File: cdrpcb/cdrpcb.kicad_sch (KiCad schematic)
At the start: 42 parts, among them J1 Conn_02x04_Odd_Even, J2 Conn_01x03, J3 Conn_01x03, J4 Conn_01x03, J5 Conn_01x03, J6 Conn_01x03, J7 Conn_01x06, J8 Conn_01x05, J9 Conn_01x03, SW1 SW_Push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

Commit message: update cdrpcb
bno055 footprints
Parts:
- removed SW1, SW2, SW3, SW4, SW5: SW_Push, Button_Switch_THT:SW_PUSH_6mm, symbol Switch:SW_Push
- added SW1, SW3: SW_Push, Connector_PinHeader_2.54mm:PinHeader_1x01_P2.54mm_Vertical, symbol Connector:Conn_01x01_Pin
- added SW2, SW4, SW5: SW_Push, Connector_PinHeader_2.54mm:PinHeader_1x02_P2.54mm_Vertical, symbol Connector:Conn_01x01_Pin
- added TP1: ~, TP4056:TP4056-18650, symbol TP4056:TP4056
- C1: footprint Capacitor_THT:CP_Radial_D4.0mm_P1.50mm -> Connector_PinHeader_2.54mm:PinHeader_1x02_P2.54mm_Horizontal
- U1: footprint Package_LGA:LGA-28_5.2x3.8mm_P0.5mm -> Library:BNO055_Breakout
- U2: footprint SC0918:MODULE_SC0918 -> RP2040_SC0918:MODULE_SC0918
- U3: footprint PDIP8_300MC_MCH -> 25LC1024:PDIP8_300MC_MCH
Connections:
- net RST: now also SW1.1 (Pin_1)
- net SW0: now also SW2.1 (Pin_1)
- net SW1: now also SW3.1 (Pin_1)
- net SW2: now also SW4.1 (Pin_1), SW5.1 (Pin_1)

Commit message: cdrpcb3
Started routing
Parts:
- removed C6, C7: 100nF, Capacitor_THT:CP_Radial_D4.0mm_P1.50mm, symbol Device:C
- removed J6: Conn_01x03, Connector_PinHeader_2.54mm:PinHeader_1x03_P2.54mm_Vertical, symbol Connector_Generic:Conn_01x03
- removed J8: Conn_01x05, Connector_PinHeader_2.54mm:PinHeader_1x05_P2.54mm_Vertical, symbol Connector_Generic:Conn_01x05
- removed SW1, SW3: SW_Push, Connector_PinHeader_2.54mm:PinHeader_1x01_P2.54mm_Vertical, symbol Connector:Conn_01x01_Pin
- removed SW2, SW4, SW5: SW_Push, Connector_PinHeader_2.54mm:PinHeader_1x02_P2.54mm_Vertical, symbol Connector:Conn_01x01_Pin
- removed TP1: ~, TP4056:TP4056-18650, symbol TP4056:TP4056
- removed U1: BNO055, Library:BNO055_Breakout, symbol Sensor_Motion:BNO055
- added J8: Conn_01x04, symbol Connector_Generic:Conn_01x04
- added SW1, SW2, SW3, SW4, SW5: Conn_01x02_Pin, symbol Connector:Conn_01x02_Pin
- added U2, U3: ~, Library:BNO055_Breakout, symbol Adafruit BNO055-eagle-import:BNO055_Breakout
- added U4: ~, TP4056:TP4056-18650, symbol TP4056:TP4056
- C1: footprint Connector_PinHeader_2.54mm:PinHeader_1x02_P2.54mm_Horizontal -> Capacitor_THT:CP_Radial_D4.0mm_P1.50mm
- renumbered U2 to U1, U3 to U5
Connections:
- net +3.3V: now also J8.4 (Pin_4), U2.1 (Vin), U2.2 (3Vo), U3.1 (Vin), U3.2 (3Vo)
- net GND: now also J8.3 (Pin_3), U2.3 (GND), U3.3 (GND), U4.4 (OUT-)
- net GP28_ADC2: now also U4.1 (OUT+)
- net GP6_INT: now also J8.2 (Pin_2)
- net GP7_AD0: now also J8.1 (Pin_1)
- net I2C0_SCL: now also U2.5 (SCL)
- net I2C0_SDA: now also U2.4 (SDA)
- net I2C1_SCL: now also U3.5 (SCL)
- net I2C1_SDA: now also U3.4 (SDA)
- net RST: now also SW1.1 (Pin_1), U2.6 (RST), U3.6 (RST)
- net SW0: now also SW2.1 (Pin_1)
- net SW1: now also SW3.1 (Pin_1)
- net SW2: now also SW4.1 (Pin_1), SW5.1 (Pin_1)
- net at R13.1: now also SW5.2 (Pin_2)
- net at R4.1: now also SW1.2 (Pin_2)
- net at R10.1: now also SW4.2 (Pin_2)
- net at R8.1: now also SW3.2 (Pin_2)
- net at R6.1: now also SW2.2 (Pin_2)
- no-connect marks 10 -> 9
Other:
- note removed: "ADC 2"
- note removed: "Bonus I2C"
- moved on the sheet: H1, H2

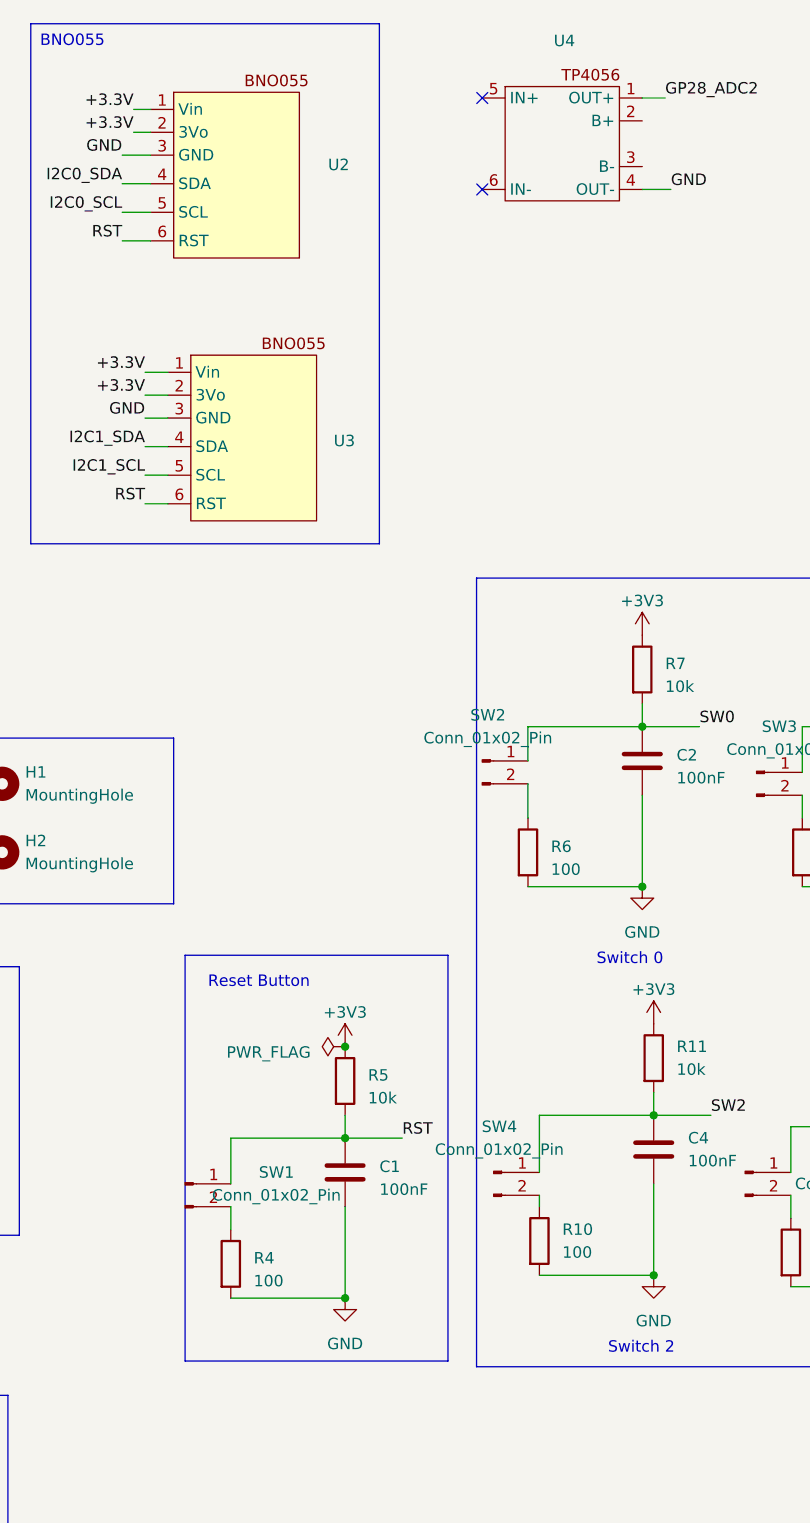
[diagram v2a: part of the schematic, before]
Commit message: cdrpcb5
centered the mounting holes
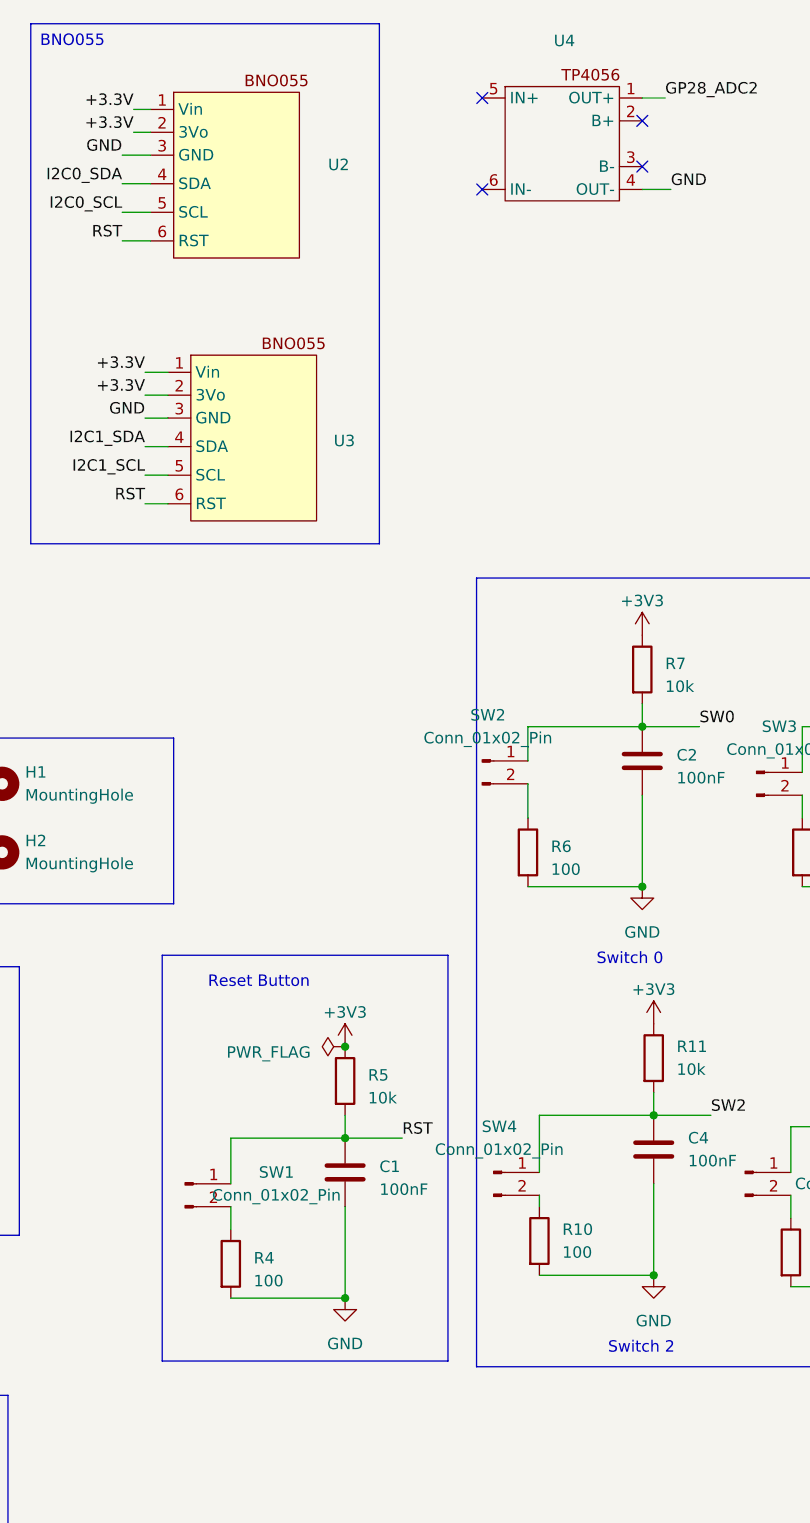
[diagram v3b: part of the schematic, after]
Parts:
- J8: footprint (none) -> Connector_PinHeader_2.54mm:PinHeader_1x04_P2.54mm_Vertical
- SW1, SW2, SW3, SW4, SW5: footprint (none) -> Connector_PinHeader_2.54mm:PinHeader_1x02_P2.54mm_Vertical
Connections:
- no-connect marks 9 -> 11
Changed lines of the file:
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@@
   )
   (no_connect (at 157.48 181.61))
+  (no_connect (at 242.57 30.48))
   (no_connect (at 224.79 22.86))
   (no_connect (at 88.265 85.725))
+  (no_connect (at 242.57 25.4))
   (no_connect (at 88.265 93.345))
   (no_connect (at 88.265 100.965))
@@
   )
   (text_box ""
-    (at 191.77 118.11 0) (size 29.21 45.085)
+    (at 189.23 118.11 0) (size 31.75 45.085)
     (stroke (width 0) (type default))
     (fill (type none))
@@
       (effects (font (size 1.27 1.27)))
     )
-    (property "Footprint" "" (at 255.27 97.79 0)
+    (property "Footprint" "Connector_PinHeader_2.54mm:PinHeader_1x02_P2.54mm_Vertical" (at 255.27 97.79 0)
       (effects (font (size 1.27 1.27)) hide)
     )
@@
       (effects (font (size 1.27 1.27)))
     )
-    (property "Footprint" "" (at 226.06 142.24 0)
+    (property "Footprint" "Connector_PinHeader_2.54mm:PinHeader_1x02_P2.54mm_Vertical" (at 226.06 142.24 0)
       (effects (font (size 1.27 1.27)) hide)
     )
@@
       (effects (font (size 1.27 1.27)))
     )
-    (property "Footprint" "" (at 254 142.24 0)
+    (property "Footprint" "Connector_PinHeader_2.54mm:PinHeader_1x02_P2.54mm_Vertical" (at 254 142.24 0)
       (effects (font (size 1.27 1.27)) hide)
     )
@@
       (effects (font (size 1.27 1.27)))
     )
-    (property "Footprint" "" (at 191.77 143.51 0)
+    (property "Footprint" "Connector_PinHeader_2.54mm:PinHeader_1x02_P2.54mm_Vertical" (at 191.77 143.51 0)
       (effects (font (size 1.27 1.27)) hide)
     )
@@
       (effects (font (size 1.27 1.27)))
     )
-    (property "Footprint" "" (at 224.79 96.52 0)
+    (property "Footprint" "Connector_PinHeader_2.54mm:PinHeader_1x02_P2.54mm_Vertical" (at 224.79 96.52 0)
       (effects (font (size 1.27 1.27)) hide)
     )
@@
       (effects (font (size 1.27 1.27)))
     )
-    (property "Footprint" "" (at 160.655 132.08 0)
-      (effects (font (size 1.27 1.27)) hide)
-    )
+    (property "Footprint" "Connector_PinHeader_2.54mm:PinHeader_1x04_P2.54mm_Vertical" (at 160.655 132.08 0)
+      (effects (font (size 1.27 1.27)) hide)
+    )
